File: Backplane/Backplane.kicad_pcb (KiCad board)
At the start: 2 copper layers, 129.5 x 120 mm, 453 parts

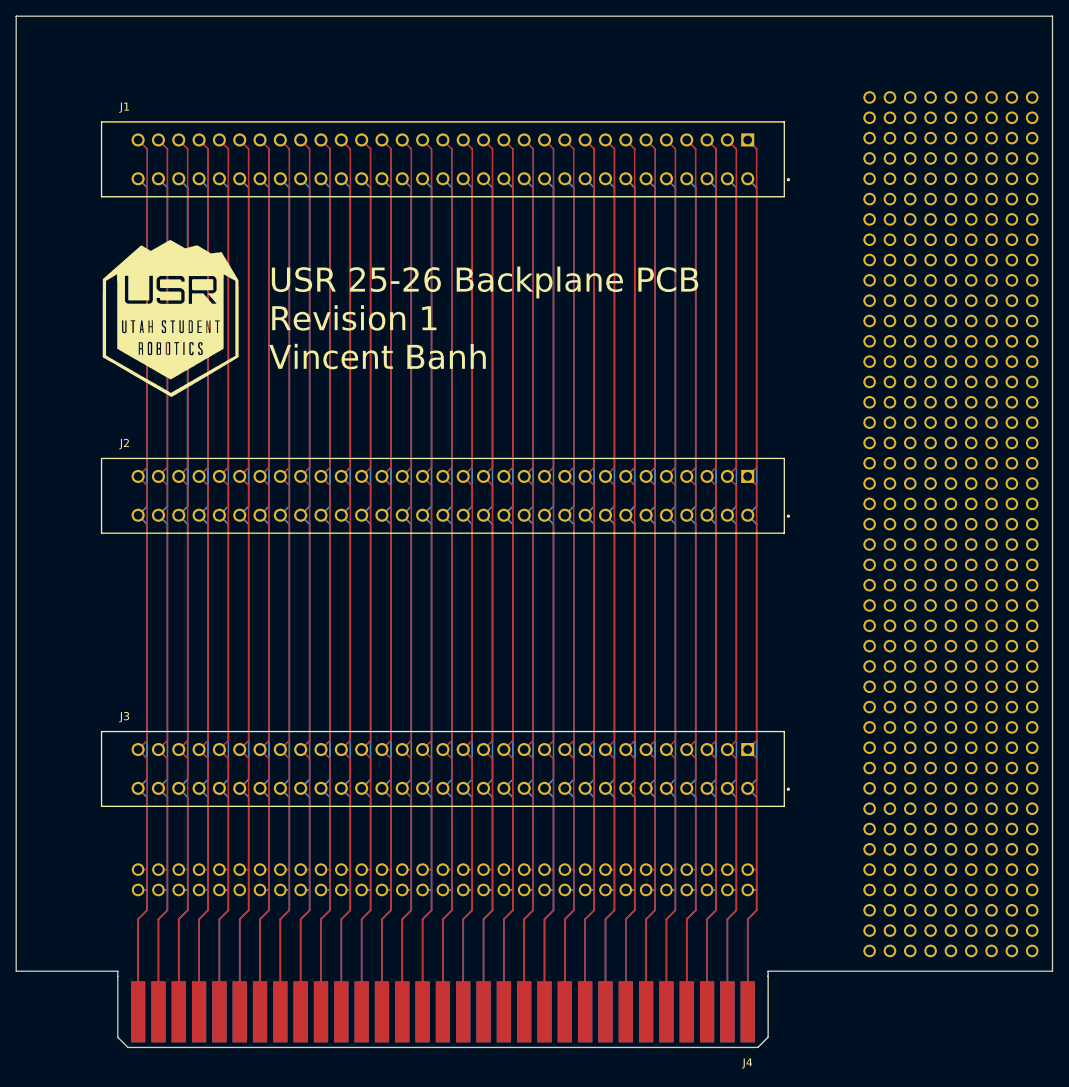
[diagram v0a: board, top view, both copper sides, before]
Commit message: Added footprints for vertical and horizontal XT-90 connectors alongside updating backplane PCB
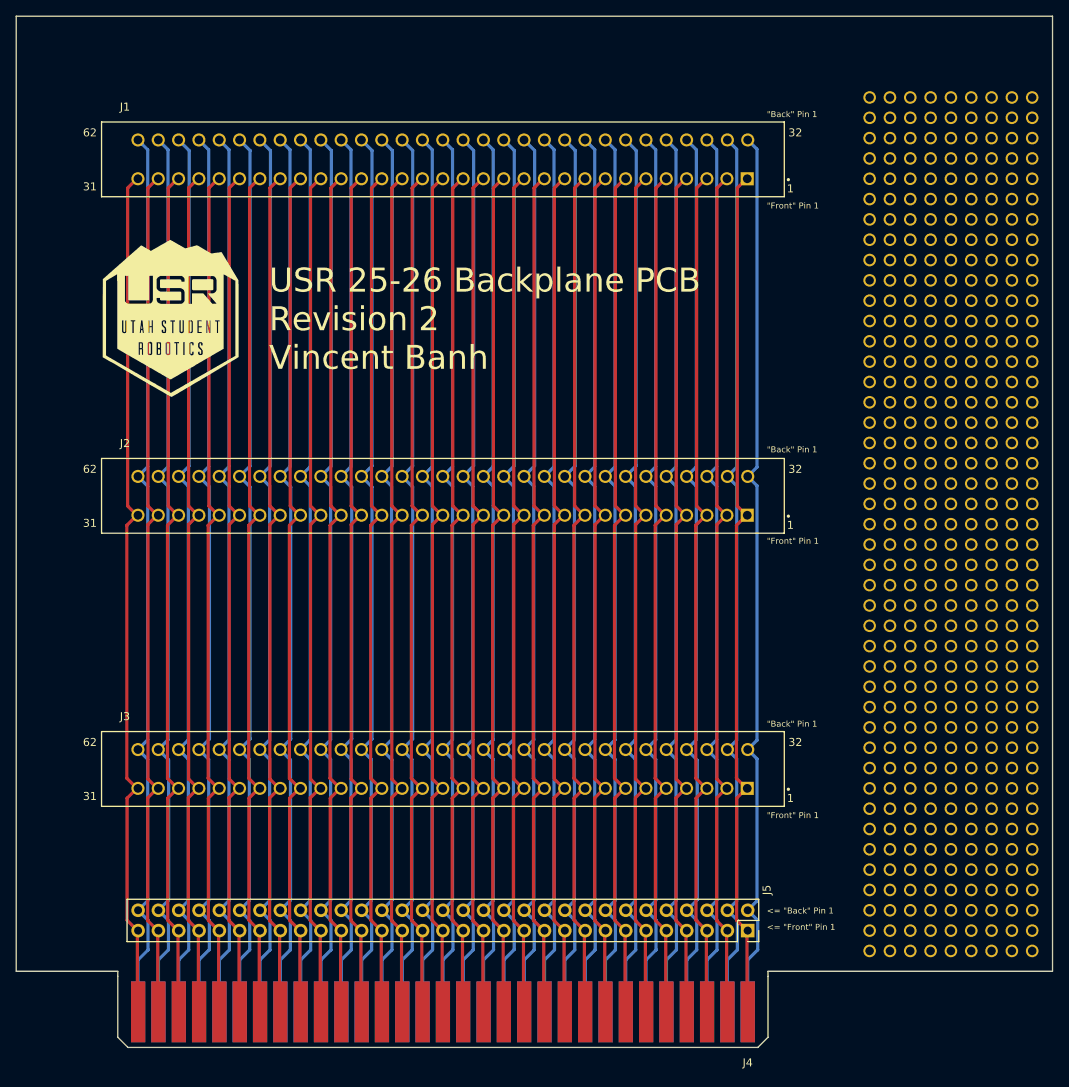
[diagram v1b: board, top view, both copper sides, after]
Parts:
- removed the ? at (105.6, 137.2)
- removed the ? at (146.2, 134.6)
- removed the ? at (136.0, 134.6)
- removed the ? at (97.9, 134.6)
- removed the ? at (123.3, 134.6)
- removed the ? at (92.9, 134.6)
- removed the ? at (148.7, 137.2)
- removed the ? at (87.8, 137.2)
- removed the ? at (120.8, 137.2)
- removed the ? at (131.0, 137.2)
- removed the ? at (97.9, 137.2)
- removed the ? at (120.8, 134.6)
- removed the ? at (133.5, 134.6)
- removed the ? at (85.2, 137.2)
- removed the ? at (110.6, 134.6)
- removed the ? at (105.6, 134.6)
- removed the ? at (148.7, 134.6)
- removed the ? at (115.7, 134.6)
- removed the ? at (125.9, 134.6)
- removed the ? at (141.1, 137.2)
- removed the ? at (133.5, 137.2)
- removed the ? at (131.0, 134.6)
- removed the ? at (100.5, 137.2)
- removed the ? at (146.2, 137.2)
- removed the ? at (125.9, 137.2)
- removed the ? at (123.3, 137.2)
- removed the ? at (115.7, 137.2)
- removed the ? at (87.8, 134.6)
- removed the ? at (156.4, 134.6)
- removed the ? at (113.2, 134.6)
- removed the ? at (92.9, 137.2)
- removed the ? at (151.3, 134.6)
- removed the ? at (108.1, 137.2)
- removed the ? at (136.0, 137.2)
- removed the ? at (118.3, 134.6)
- removed the ? at (103.0, 137.2)
- removed the ? at (156.4, 137.2)
- removed the ? at (80.2, 137.2)
- removed the ? at (138.6, 134.6)
- removed the ? at (82.7, 134.6)
- removed the ? at (113.2, 137.2)
- removed the ? at (128.4, 137.2)
- removed the ? at (90.3, 137.2)
- removed the ? at (118.3, 137.2)
- removed the ? at (80.2, 134.6)
- removed the ? at (95.4, 137.2)
- removed the ? at (151.3, 137.2)
- removed the ? at (128.4, 134.6)
- removed the ? at (141.1, 134.6)
- removed the ? at (90.3, 134.6)
- removed the ? at (82.7, 137.2)
- removed the ? at (153.8, 137.2)
- removed the ? at (103.0, 134.6)
- removed the ? at (153.8, 134.6)
- removed the ? at (138.6, 137.2)
- removed the ? at (143.7, 134.6)
- removed the ? at (95.4, 134.6)
- removed the ? at (85.2, 134.6)
- removed the ? at (110.6, 137.2)
- removed the ? at (100.5, 134.6)
- removed the ? at (143.7, 137.2)
- removed the ? at (108.1, 134.6)
- added J5: ~, USR:PinHeader_2x31_P2.54mm_Vertical_BACKPLANE, F.Cu at (156.4, 141.0)
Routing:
- net /60: track 146.7 -> 113.1 mm
- net /59: track 146.7 -> 113.2 mm
- net /38: track 138.8 -> 113.1 mm
- net /51: track 106.9 -> 113.2 mm
- net /57: track 106.9 -> 113.2 mm
- net /49: track 106.9 -> 113.2 mm
- net /55: track 106.9 -> 113.2 mm
- net /50: track 106.9 -> 113.2 mm
- net /44: track 106.9 -> 113.2 mm
- net /35: track 106.9 -> 113.1 mm
- net /43: track 106.9 -> 113.1 mm
- net /53: track 106.9 -> 113.1 mm
- net /46: track 106.9 -> 113.1 mm
- net /56: track 106.9 -> 113.1 mm
- net /41: track 106.9 -> 113.1 mm
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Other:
- board text added: "<= {dblquote}Back{dblquote} Pin 1"
- board text added: "<= {dblquote}Front{dblquote} Pin 1"
- board text added: "USR 25-26 Backplane PCB Revision 2 Vincent Banh"
- board text added: "{dblquote}Back{dblquote} Pin 1"
- board text added: "{dblquote}Front{dblquote} Pin 1"
- board text removed: "USR 25-26 Backplane PCB Revision 1 Vincent Banh"
